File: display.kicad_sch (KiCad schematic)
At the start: 4 parts, among them J5 Conn_01x24_Socket, U5 FAN5331SX

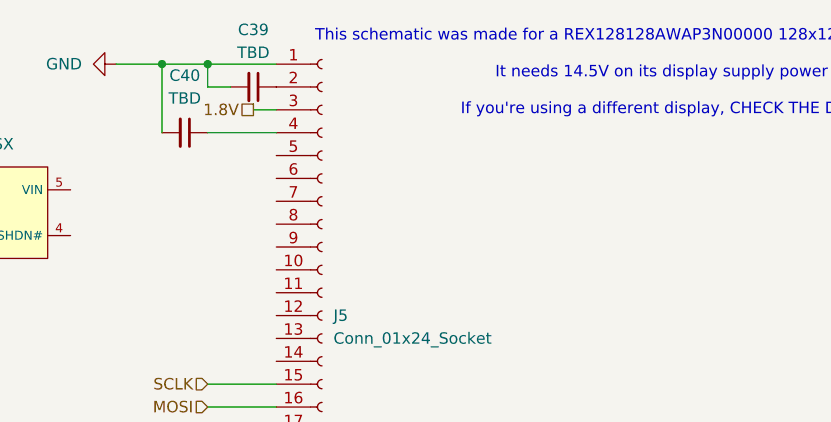
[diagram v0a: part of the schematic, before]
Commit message: re-integrate all components + add BT antenna
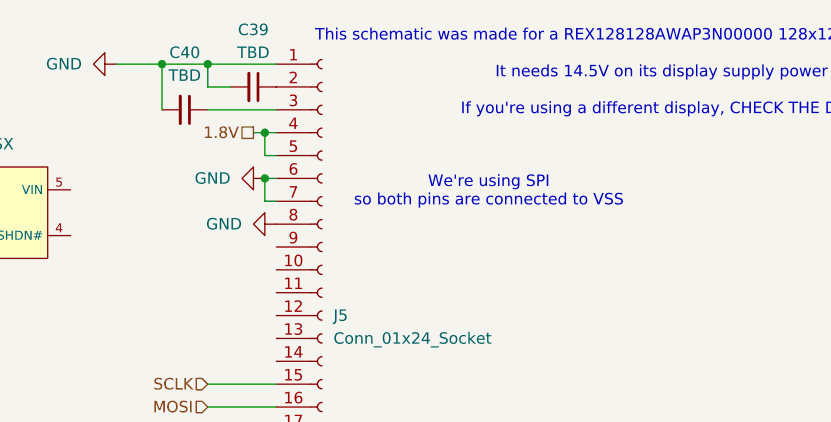
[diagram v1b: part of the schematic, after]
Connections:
- net 1.8V: now also J5.4 (Pin_4), J5.5 (Pin_5); no longer J5.3 (Pin_3)
- net GND: now also J5.6 (Pin_6), J5.7 (Pin_7), J5.8 (Pin_8)
- net at C40.1: now also J5.3 (Pin_3); no longer J5.4 (Pin_4)
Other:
- note added: "We're using SPI so both pins are connected to VSS"
- moved on the sheet: C40
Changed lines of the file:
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@@
 	(paper "A4")
+	(junction
+		(at 90.17 74.93)
+		(diameter 0)
+		(color 0 0 0 0)
+	)
+	(junction
+		(at 90.17 69.85)
+		(diameter 0)
+		(color 0 0 0 0)
+	)
 	(junction
 		(at 78.74 62.23)
@@
 	(wire
 		(pts
-			(xy 88.9 67.31) (xy 91.44 67.31)
-		)
-		(stroke
-			(width 0)
-			(type default)
-		)
-	)
-	(wire
-		(pts
 			(xy 83.82 64.77) (xy 83.82 62.23)
 		)
@@
 	(wire
 		(pts
-			(xy 83.82 69.85) (xy 91.44 69.85)
+			(xy 90.17 69.85) (xy 91.44 69.85)
+		)
+		(stroke
+			(width 0)
+			(type default)
+		)
+	)
+	(wire
+		(pts
+			(xy 90.17 77.47) (xy 90.17 74.93)
+		)
+		(stroke
+			(width 0)
+			(type default)
+		)
+	)
+	(wire
+		(pts
+			(xy 90.17 72.39) (xy 90.17 69.85)
 		)
 		(stroke
@@
 	(wire
 		(pts
-			(xy 78.74 62.23) (xy 78.74 69.85)
+			(xy 91.44 72.39) (xy 90.17 72.39)
+		)
+		(stroke
+			(width 0)
+			(type default)
+		)
+	)
+	(wire
+		(pts
+			(xy 83.82 67.31) (xy 91.44 67.31)
+		)
+		(stroke
+			(width 0)
+			(type default)
+		)
+	)
+	(wire
+		(pts
+			(xy 78.74 62.23) (xy 78.74 67.31)
 		)
 		(stroke
@@
 	(wire
 		(pts
+			(xy 91.44 77.47) (xy 90.17 77.47)
+		)
+		(stroke
+			(width 0)
+			(type default)
+		)
+	)
+	(wire
+		(pts
+			(xy 88.9 69.85) (xy 90.17 69.85)
+		)
+		(stroke
+			(width 0)
+			(type default)
+		)
+	)
+	(wire
+		(pts
 			(xy 78.74 62.23) (xy 83.82 62.23)
 		)
@@
 		(pts
 			(xy 83.82 97.79) (xy 91.44 97.79)
+		)
+		(stroke
+			(width 0)
+			(type default)
+		)
+	)
+	(wire
+		(pts
+			(xy 90.17 74.93) (xy 91.44 74.93)
 		)
 		(stroke
@@
 		)
 	)
+	(text "We're using SPI\nso both pins are connected to VSS"
+		(exclude_from_sim no)
+		(at 115.062 76.454 0)
+		(effects
+			(font
+				(size 1.27 1.27)
+			)
+		)
+	)
+	(hierarchical_label "1.8V"
+		(shape passive)
+		(at 88.9 69.85 180)
+		(fields_autoplaced yes)
+		(effects
+			(font
+				(size 1.27 1.27)
+			)
+			(justify right)
+		)
+	)
 	(hierarchical_label "MOSI"
 		(shape input)
 		(at 83.82 100.33 180)
-		(fields_autoplaced yes)
-		(effects
-			(font
-				(size 1.27 1.27)
-			)
-			(justify right)
-		)
-	)
-	(hierarchical_label "1.8V"
-		(shape passive)
-		(at 88.9 67.31 180)
 		(fields_autoplaced yes)
 		(effects
@@
 	(symbol
 		(lib_id "Device:C_Small")
-		(at 81.28 69.85 270)
+		(at 81.28 67.31 270)
 		(unit 1)
 		(exclude_from_sim no)
@@
 		(fields_autoplaced yes)
 		(property "Reference" "C40"
+			(at 81.2736 60.96 90)
+			(effects
+				(font
+					(size 1.27 1.27)
+				)
+			)
+		)
+		(property "Value" "TBD"
 			(at 81.2736 63.5 90)
 			(effects
@@
 			)
 		)
-		(property "Value" "TBD"
-			(at 81.2736 66.04 90)
-			(effects
-				(font
-					(size 1.27 1.27)
-				)
-			)
-		)
 		(property "Footprint" ""
-			(at 81.28 69.85 0)
+			(at 81.28 67.31 0)
 			(effects
 				(font
@@
 		)
 		(property "Datasheet" "~"
-			(at 81.28 69.85 0)
+			(at 81.28 67.31 0)
 			(effects
 				(font
@@
 		)
 		(property "Description" "Unpolarized capacitor, small symbol"
-			(at 81.28 69.85 0)
+			(at 81.28 67.31 0)
 			(effects
 				(font
@@
 					(unit 1)
 				)
+			)
+		)
+	)
+	(symbol
+		(lib_id "power:GND")
+		(at 91.44 80.01 270)
+		(unit 1)
+		(exclude_from_sim no)
+		(in_bom yes)
+		(on_board yes)
+		(dnp no)
+		(fields_autoplaced yes)
+		(property "Reference" "#PWR039"
+			(at 85.09 80.01 0)
+			(effects
+				(font
+					(size 1.27 1.27)
+				)
+				(hide yes)
+			)
+		)
+		(property "Value" "GND"
+			(at 87.63 80.0099 90)
+			(effects
+				(font
+					(size 1.27 1.27)
+				)
+				(justify right)
+			)
+		)
+		(property "Footprint" ""
+			(at 91.44 80.01 0)
+			(effects
+				(font
+					(size 1.27 1.27)
+				)
+				(hide yes)
+			)
+		)
+		(property "Datasheet" ""
+			(at 91.44 80.01 0)
+			(effects
+				(font
+					(size 1.27 1.27)
+				)
+				(hide yes)
+			)
+		)
+		(property "Description" "Power symbol creates a global label with name \"GND\" , ground"
+			(at 91.44 80.01 0)
+			(effects
+				(font
+					(size 1.27 1.27)
+				)
+				(hide yes)
+			)
+		)
+		(pin "1"
+		)
+		(instances
+			(project "OpenBikeComputer"
+				(path "/110ea5a2-03d6-426d-b79f-fcb4ea6cee9d/67feebfd-a6ea-41ab-b461-383184077ed3"
+					(reference "#PWR039")
+					(unit 1)
+				)
+			)
+		)
+	)
+	(symbol
+		(lib_id "power:GND")
+		(at 90.17 74.93 270)
+		(unit 1)
+		(exclude_from_sim no)
+		(in_bom yes)
+		(on_board yes)
+		(dnp no)
+		(fields_autoplaced yes)
+		(property "Reference" "#PWR038"
+			(at 83.82 74.93 0)
+			(effects
+				(font
+					(size 1.27 1.27)
+				)
+				(hide yes)
+			)
+		)
+		(property "Value" "GND"
+			(at 86.36 74.9299 90)
+			(effects
+				(font
+					(size 1.27 1.27)
+				)
+				(justify right)
+			)
+		)
+		(property "Footprint" ""
+			(at 90.17 74.93 0)
+			(effects
+				(font
+					(size 1.27 1.27)
+				)
+				(hide yes)
+			)
+		)
+		(property "Datasheet" ""
+			(at 90.17 74.93 0)
+			(effects
+				(font
+					(size 1.27 1.27)
+				)
+				(hide yes)
+			)
+		)
+		(property "Description" "Power symbol creates a global label with name \"GND\" , ground"
+			(at 90.17 74.93 0)
+			(effects
+				(font
+					(size 1.27 1.27)
+				)
+				(hide yes)
+			)
+		)
+		(pin "1"
+		)
+		(instances
+			(project "OpenBikeComputer"
+				(path "/110ea5a2-03d6-426d-b79f-fcb4ea6cee9d/67feebfd-a6ea-41ab-b461-383184077ed3"
+					(reference "#PWR038")
+					(unit 1)
+				)

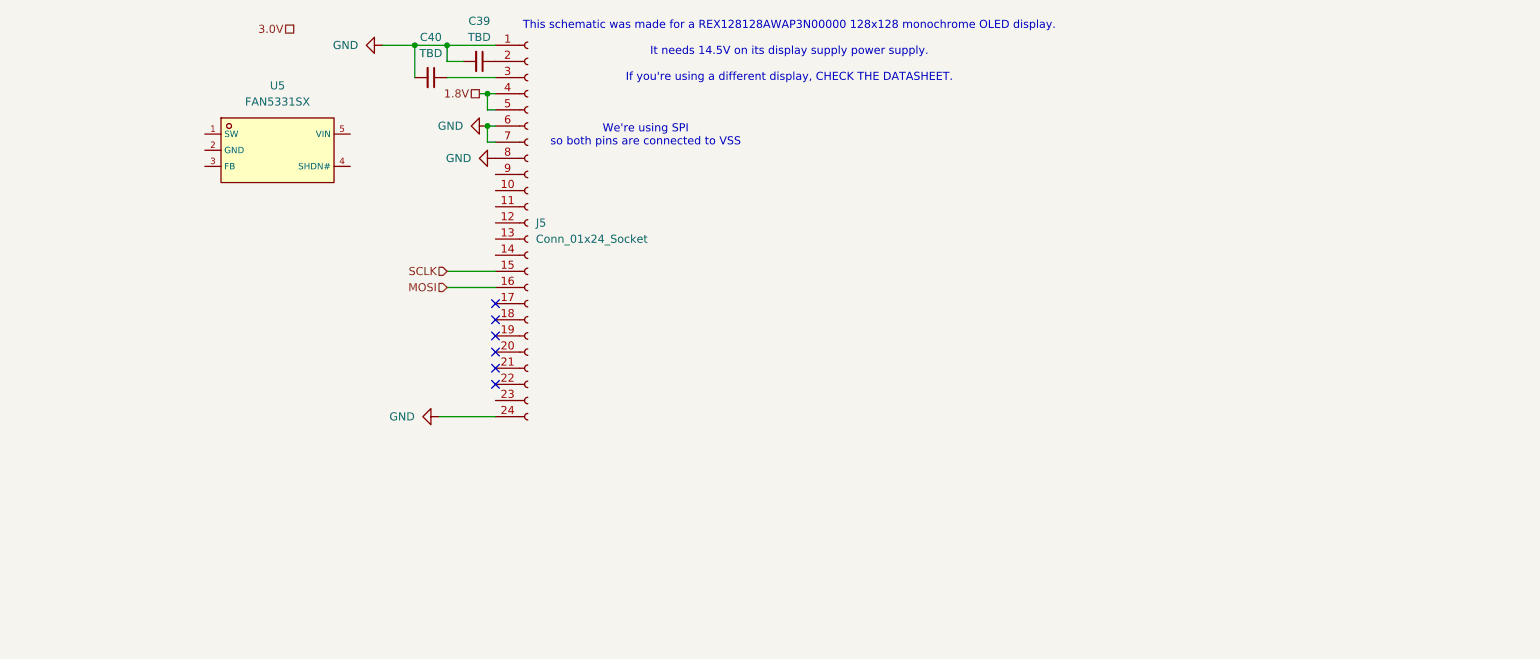
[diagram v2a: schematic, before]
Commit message: finish oled driver circuit
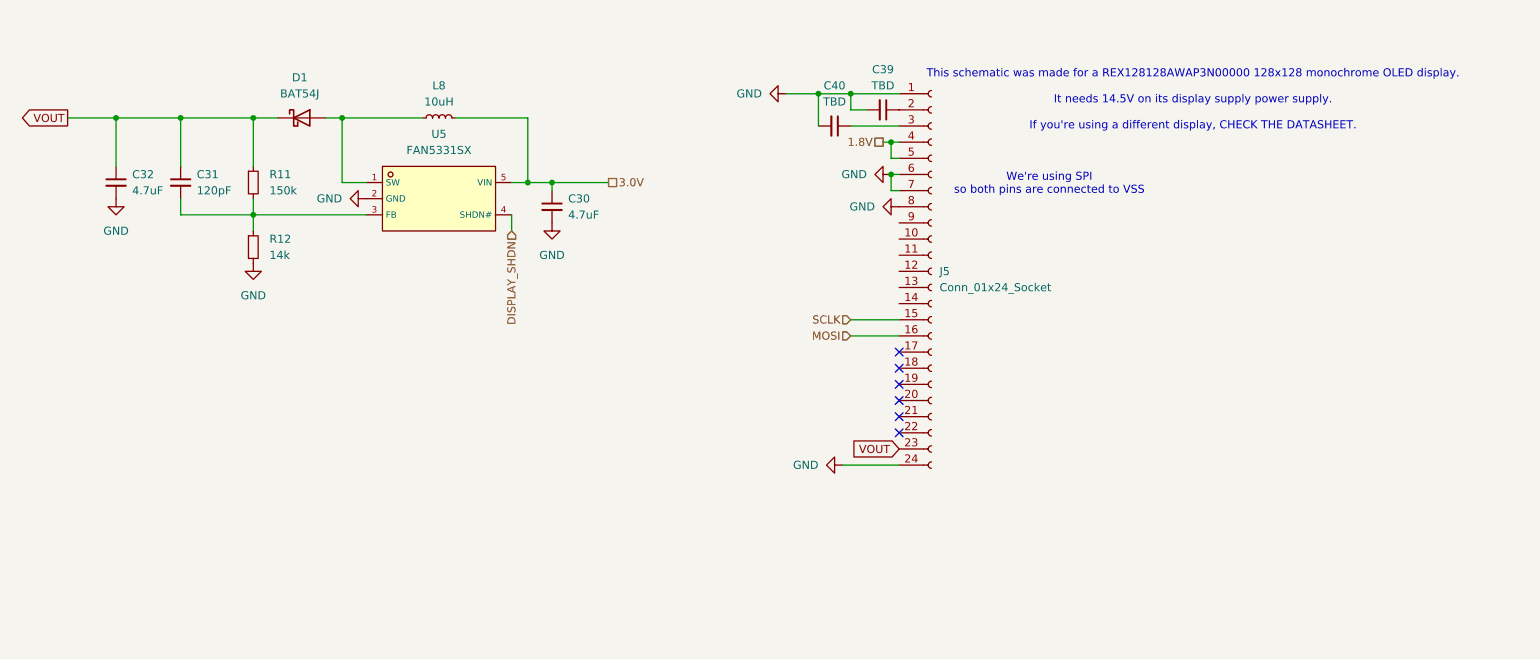
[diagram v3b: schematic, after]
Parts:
- added C30, C32: 4.7uF, Capacitor_SMD:C_0603_1608Metric, symbol Device:C_Small
- added C31: 120pF, Capacitor_SMD:C_0603_1608Metric, symbol Device:C_Small
- added D1: BAT54J, Diode_SMD:D_SOD-323F, symbol Diode:BAT54J
- added L8: 10uH, symbol Device:L_Small
- added R11: 150k, symbol Device:R_Small
- added R12: 14k, symbol Device:R_Small
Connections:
- net 3.0V: now also U5.5 (VIN), C30.1, L8.2
- net GND: now also U5.2 (GND), C30.2, C32.2, R12.2
- net at U5.1 (SW): now also D1.2 (A), L8.1
- net at U5.3 (FB): now also C31.2, R11.2, R12.1
- net DISPLAY_SHDN: now reaches U5.4 (SHDN#)
- net VOUT: now reaches J5.23 (Pin_23)
- net VOUT: now also C31.1, C32.1, D1.1 (K), R11.1
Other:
- moved on the sheet: C39, C40, J5, U5

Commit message: begin new board
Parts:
- removed J5: Conn_01x24_Socket, Connector_FFC-FPC:TE_2-84952-4_1x24-1MP_P1.0mm_Horizontal, symbol Connector:Conn_01x24_Socket
- added J3: Conn_01x30_Socket, Library:CON_541043031_MOL, symbol Connector:Conn_01x30_Socket
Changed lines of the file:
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@@
-	)
-	(symbol
-		(lib_id "Connector:Conn_01x24_Socket")
-		(at 160.02 97.79 0)
-		(unit 1)
-		(exclude_from_sim no)
-		(in_bom yes)
-		(on_board yes)
-		(dnp no)
-		(fields_autoplaced yes)
-		(property "Reference" "J5"
-			(at 161.29 97.7899 0)
-			(effects
-				(font
-					(size 1.27 1.27)
-				)
-				(justify left)
-			)
-		)
-		(property "Value" "Conn_01x24_Socket"
-			(at 161.29 100.3299 0)
-			(effects
-				(font
-					(size 1.27 1.27)
-				)
-				(justify left)
-			)
-		)
-		(property "Footprint" "Connector_FFC-FPC:TE_2-84952-4_1x24-1MP_P1.0mm_Horizontal"
-			(at 160.02 97.79 0)
-			(effects
-				(font
-					(size 1.27 1.27)
-				)
-				(hide yes)
-			)
-		)
-		(property "Datasheet" "~"
-			(at 160.02 97.79 0)
-			(effects
-				(font
-					(size 1.27 1.27)
-				)
-				(hide yes)
-			)
-		)
-		(property "Description" "Generic connector, single row, 01x24, script generated"
-			(at 160.02 97.79 0)
-			(effects
-				(font
-					(size 1.27 1.27)
-				)
-				(hide yes)
-			)
-		)
-		(pin "6"
-		)
-		(pin "9"
-		)
-		(pin "21"
-		)
-		(pin "2"
-		)
-		(pin "18"
-		)
-		(pin "22"
-		)
-		(pin "24"
-		)
-		(pin "19"
-		)
-		(pin "23"
-		)
-		(pin "8"
-		)
-		(pin "7"
-		)
-		(pin "13"
-		)
-		(pin "14"
-		)
-		(pin "15"
-		)
-		(pin "1"
-		)
-		(pin "10"
-		)
-		(pin "5"
-		)
-		(pin "12"
-		)
-		(pin "20"
-		)
-		(pin "16"
-		)
-		(pin "11"
-		)
-		(pin "17"
-		)
-		(pin "3"
-		)
-		(pin "4"
-		)
-		(instances
-			(project ""
-				(path "/110ea5a2-03d6-426d-b79f-fcb4ea6cee9d/67feebfd-a6ea-41ab-b461-383184077ed3"
-					(reference "J5")
-					(unit 1)
-				)
-			)
-		)
 	)
 	(symbol
@@
 					(unit 1)
 				)
+			)
+		)
+	)
+	(symbol
+		(lib_id "Connector:Conn_01x30_Socket")
+		(at 224.79 118.11 0)
+		(unit 1)
+		(exclude_from_sim no)
+		(in_bom yes)
+		(on_board yes)
+		(dnp no)
+		(fields_autoplaced yes)
+		(property "Reference" "J3"
+			(at 226.06 118.1099 0)
+			(effects
+				(font
+					(size 1.27 1.27)
+				)
+				(justify left)
+			)
+		)
+		(property "Value" "Conn_01x30_Socket"
+			(at 226.06 120.6499 0)
+			(effects
+				(font
+					(size 1.27 1.27)
+				)
+				(justify left)
+			)
+		)
+		(property "Footprint" "Library:CON_541043031_MOL"
+			(at 224.79 118.11 0)
+			(effects
+				(font
+					(size 1.27 1.27)
+				)
+				(hide yes)
+			)
+		)
+		(property "Datasheet" "~"
+			(at 224.79 118.11 0)
+			(effects
+				(font
+					(size 1.27 1.27)
+				)
+				(hide yes)
+			)
+		)
+		(property "Description" "Generic connector, single row, 01x30, script generated"
+			(at 224.79 118.11 0)
+			(effects
+				(font
+					(size 1.27 1.27)
+				)
+				(hide yes)
+			)
+		)
+		(pin "6"
+		)
+		(pin "24"
+		)
+		(pin "8"
+		)
+		(pin "15"
+		)
+		(pin "5"
+		)
+		(pin "23"
+		)
+		(pin "28"
+		)
+		(pin "16"
+		)
+		(pin "17"
+		)
+		(pin "7"
+		)
+		(pin "9"
+		)
+		(pin "21"
+		)
+		(pin "13"
+		)
+		(pin "1"
+		)
+		(pin "27"
+		)
+		(pin "26"
+		)
+		(pin "22"
+		)
+		(pin "29"
+		)
+		(pin "20"
+		)
+		(pin "2"
+		)
+		(pin "10"
+		)
+		(pin "19"
+		)
+		(pin "3"
+		)
+		(pin "18"
+		)
+		(pin "14"
+		)
+		(pin "4"
+		)
+		(pin "11"
+		)
+		(pin "30"
+		)
+		(pin "25"
+		)
+		(pin "12"
+		)
+		(instances
+			(project ""
+				(path "/110ea5a2-03d6-426d-b79f-fcb4ea6cee9d/67feebfd-a6ea-41ab-b461-383184077ed3"
+					(reference "J3")
+					(unit 1)
+				)

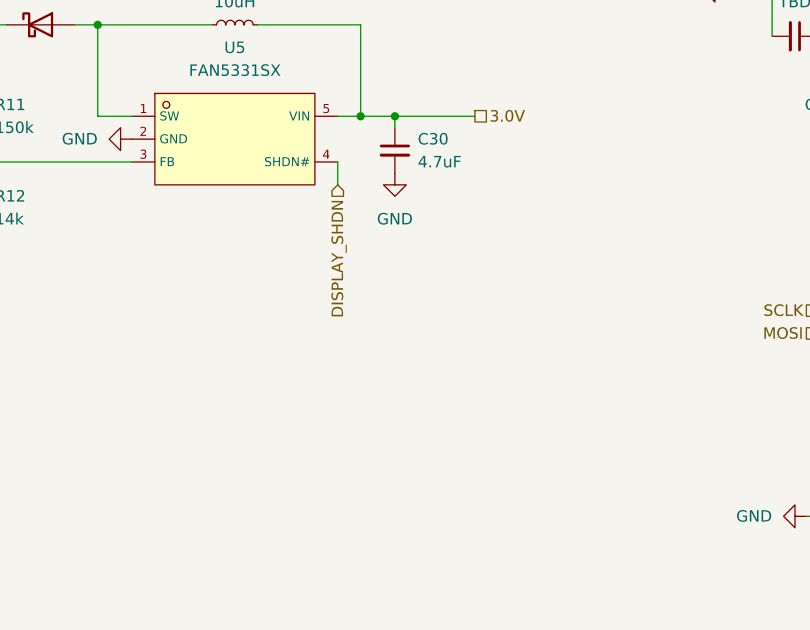
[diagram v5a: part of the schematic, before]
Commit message: add lots of test points
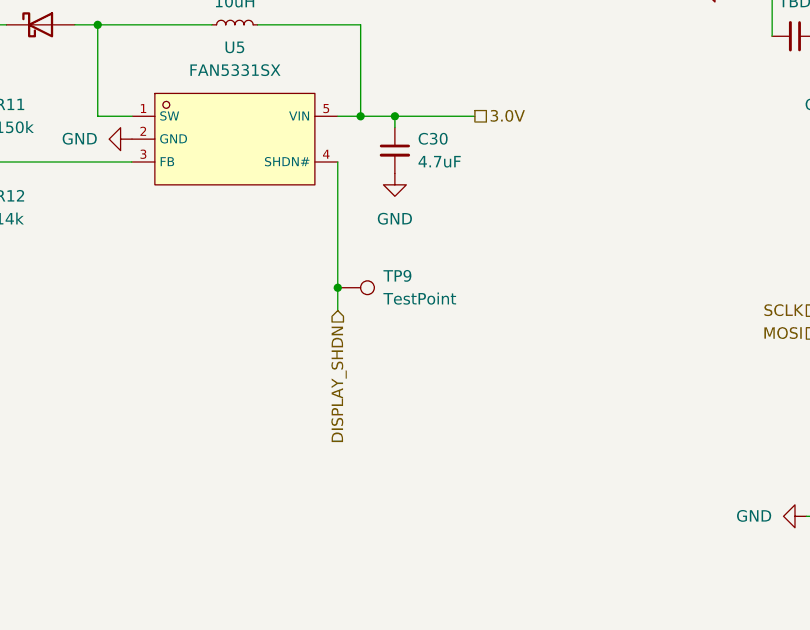
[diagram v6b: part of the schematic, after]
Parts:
- added TP9: TestPoint, symbol Connector:TestPoint
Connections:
- net DISPLAY_SHDN: now also TP9.1
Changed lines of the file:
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@@
+	)
+	(junction
+		(at 93.98 102.87)
+		(diameter 0)
+		(color 0 0 0 0)
 	)
 	(junction
@@
 	(wire
 		(pts
-			(xy 93.98 91.44) (xy 93.98 88.9)
+			(xy 93.98 105.41) (xy 93.98 102.87)
 		)
 		(stroke
@@
 		(pts
 			(xy 93.98 83.82) (xy 96.52 83.82)
+		)
+		(stroke
+			(width 0)
+			(type default)
+		)
+	)
+	(wire
+		(pts
+			(xy 93.98 102.87) (xy 93.98 88.9)
 		)
 		(stroke
@@
 	(hierarchical_label "DISPLAY_SHDN"
 		(shape input)
-		(at 93.98 91.44 270)
+		(at 93.98 105.41 270)
 		(fields_autoplaced yes)
 		(effects
@@
 					(unit 1)
 				)
+			)
+		)
+	)
+	(symbol
+		(lib_id "Connector:TestPoint")
+		(at 93.98 102.87 270)
+		(unit 1)
+		(exclude_from_sim no)
+		(in_bom yes)
+		(on_board yes)
+		(dnp no)
+		(fields_autoplaced yes)
+		(property "Reference" "TP9"
+			(at 99.06 101.5999 90)
+			(effects
+				(font
+					(size 1.27 1.27)
+				)
+				(justify left)
+			)
+		)
+		(property "Value" "TestPoint"
+			(at 99.06 104.1399 90)
+			(effects
+				(font
+					(size 1.27 1.27)
+				)
+				(justify left)
+			)
+		)
+		(property "Footprint" ""
+			(at 93.98 107.95 0)
+			(effects
+				(font
+					(size 1.27 1.27)
+				)
+				(hide yes)
+			)
+		)
+		(property "Datasheet" "~"
+			(at 93.98 107.95 0)
+			(effects
+				(font
+					(size 1.27 1.27)
+				)
+				(hide yes)
+			)
+		)
+		(property "Description" "test point"
+			(at 93.98 102.87 0)
+			(effects
+				(font
+					(size 1.27 1.27)
+				)
+				(hide yes)
+			)
+		)
+		(pin "1"
+		)
+		(instances
+			(project "OpenBikeComputer"
+				(path "/110ea5a2-03d6-426d-b79f-fcb4ea6cee9d/67feebfd-a6ea-41ab-b461-383184077ed3"
+					(reference "TP9")
+					(unit 1)
+				)
